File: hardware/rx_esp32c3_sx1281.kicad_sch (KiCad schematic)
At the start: 43 parts, among them U1 ESP32-C3FH4, U2 TLV75533PDQNR, U3 SX1281IMLTRT, X1 CJ17-400001010B20

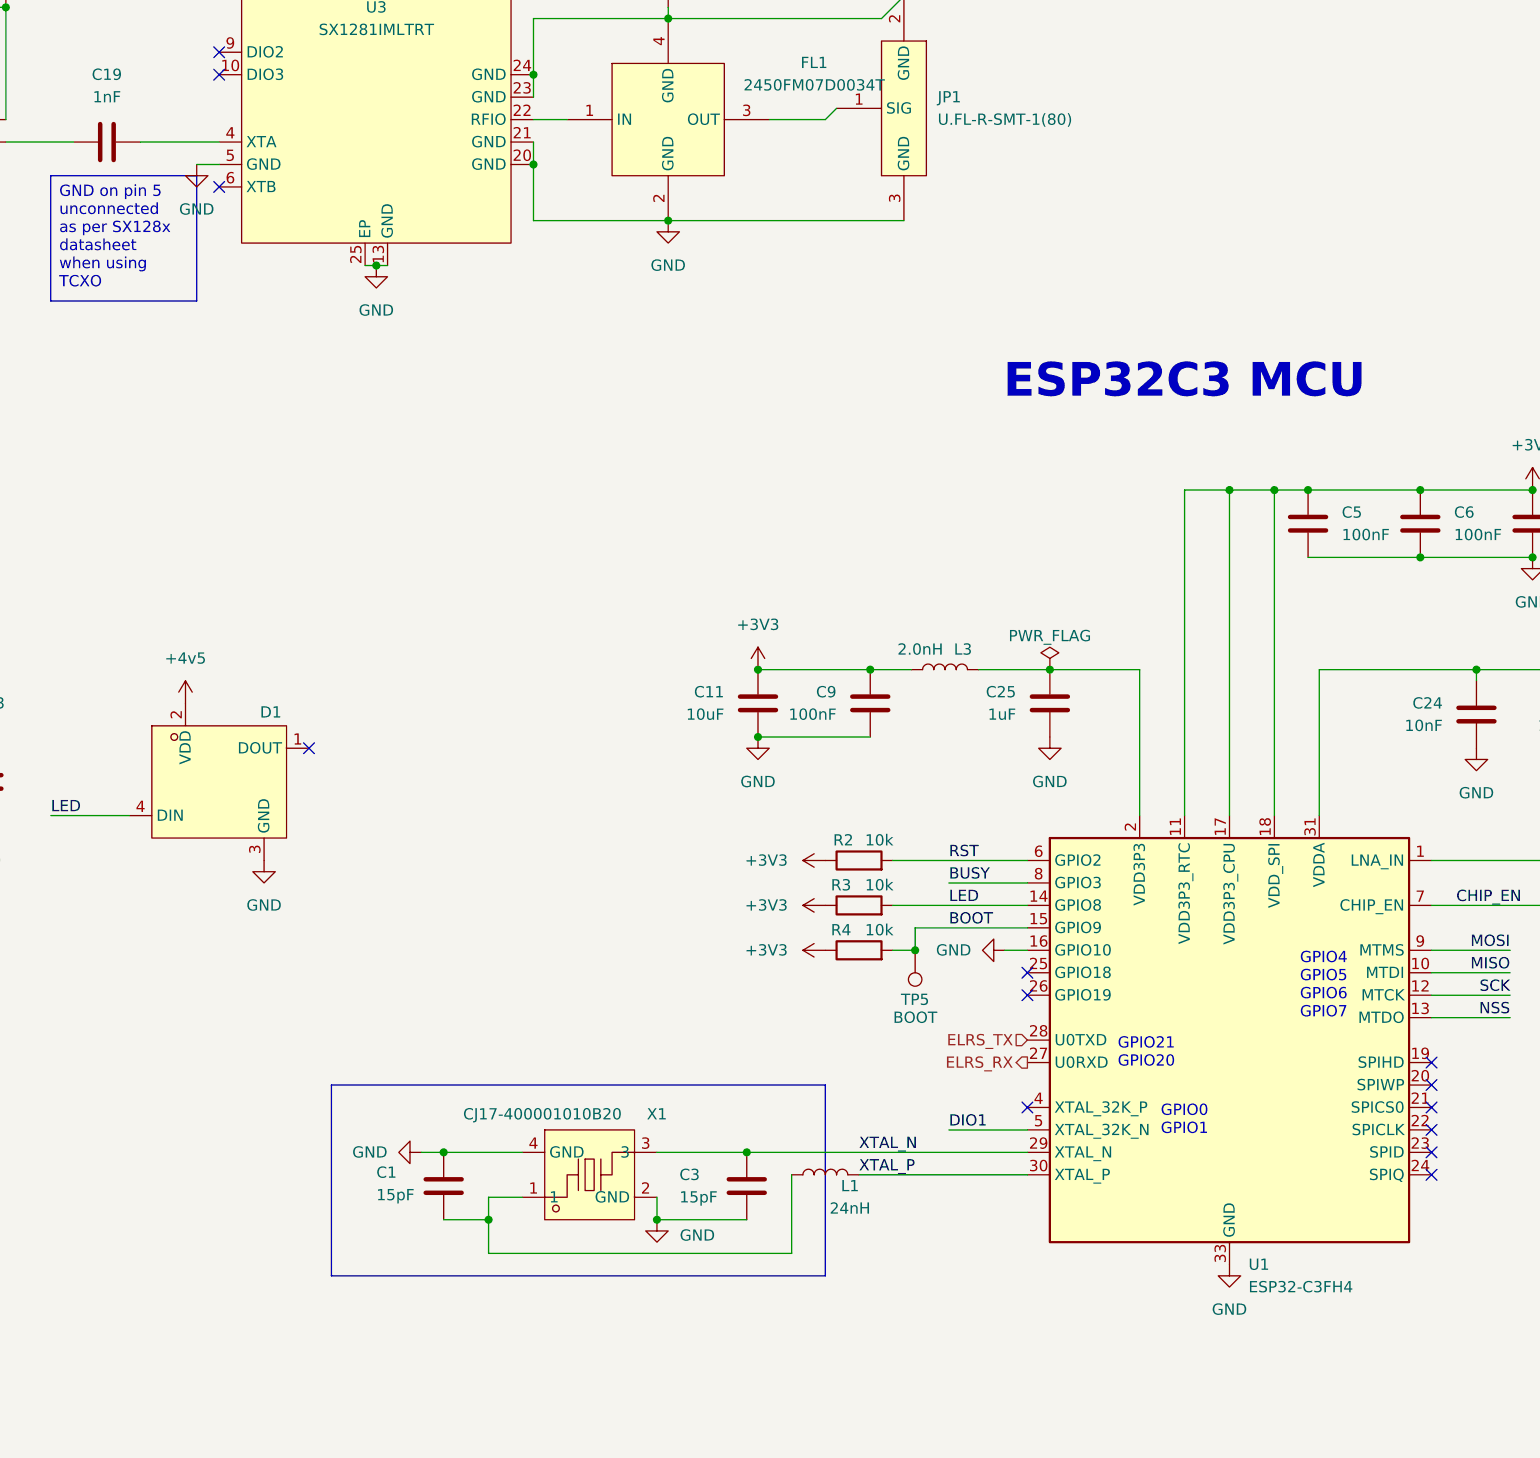
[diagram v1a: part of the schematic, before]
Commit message: One board from the owner's 2026-08-22 Base and Core, BMP580 baro (#26)
The board is rebuilt from d81e559 (the hand-routed Base recovered from KiCad
local history and the hand-routed Core of 1fe3d21) plus the always-on +10V of
9aba717, instead of the agent-reworked 8fa8d7b. Both layouts sit side by side
in hardware/OpenAIO.kicad_pcb with all routing kept (2513 tracks, 1577 vias),
on the OpenAIO-Whoop 8L HDI stackup.

- Schematic: Core_Interface (J90/J91 LGA) removed; U26 BMP580 + C107/C108 on
  I2C0 at 0x47 (Betaflight BMP5xx default). Netlist otherwise identical to
  9aba717; ERC 31 errors, the 9aba717 baseline.
- Board: Base netclasses and severities; rule area "Core layout" keeps the
  Core's 0.09 line standard. DRC: 3 errors (USB1 peg), 37 unconnected (links).
- lib.pretty footprints replaced by the board instances; BMP580 imported with
  easyeda2kicad (LCSC C22391138).
- Not carried from 8fa8d7b: TXU0101 LED-strip buffer, +3V3_ESC, SWD pads,
  DFM edits; firmware ISSUES I2/I3 reopened.
- Docs: README pinout re-measured, AGENTS.md, research/ROUTING.md, Betaflight
  target USE_BARO_BMP580.

Co-authored-by: Stan <stan@openaio.local>
Co-authored-by: Claude Opus 5.5 <noreply@anthropic.com>
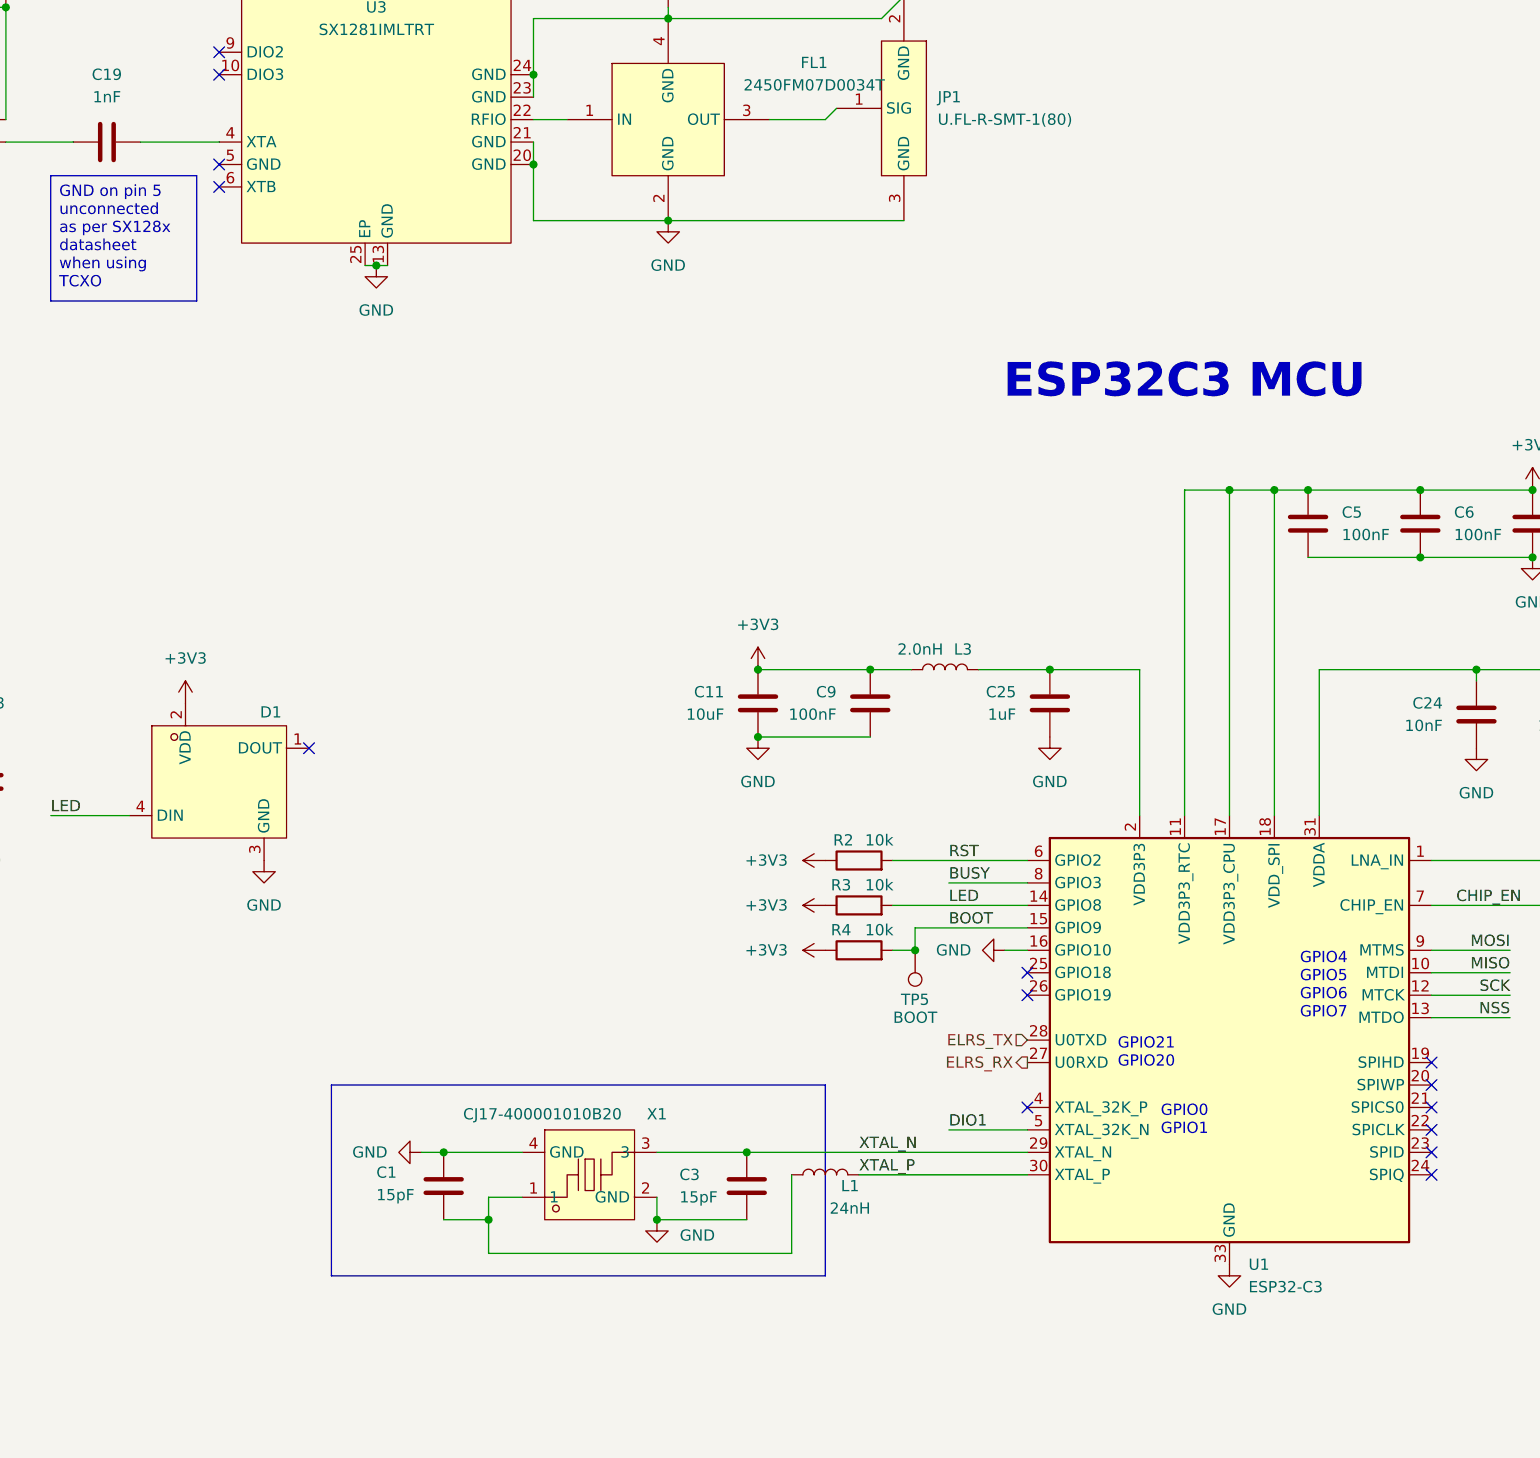
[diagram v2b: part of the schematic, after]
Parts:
- AE1: MPN 2450AT18A100E -> (none); Manufacturer JOHANSON(约翰逊) -> (none)
- C1, C3: MPN GRM0335C1H150JA01D -> (none); Manufacturer Murata Electronics -> (none)
- C10, C15, C23, C25, C28, C4: MPN GRM033R61A105ME44D -> (none); Manufacturer Murata Electronics -> (none)
- C11: MPN GRM155R60J106ME44D -> (none); Manufacturer Murata Electronics -> (none)
- C12, C13, C14, C17, C5, C6, C9: MPN GRM033R61E104KE14D -> (none); Manufacturer Murata Electronics -> (none)
- C16, C8: MPN CL05A106MQ5NUNC -> (none); Manufacturer Samsung Electro-Mechanics -> (none)
- C19: MPN 0201B102K500NT -> (none); Manufacturer FH (Guangdong Fenghua) -> (none)
- C20: MPN GRM033R60J474KE90D -> (none); Manufacturer Murata Electronics -> (none)
- C21, C22: MPN GRM0335C1H1R2BA01D -> (none); Manufacturer Murata Electronics -> (none)
- C24, C26, C27: MPN GRM033R61A103KA01J -> (none); Manufacturer Murata Electronics -> (none)
- D1: LCSC C5349953 -> (none); MPN XL-1010RGBC-2812B -> (none); Manufacturer XINGLIGHT -> (none)
- JP1: MPN U.FL-R-SMT-1(80) -> (none); Manufacturer Hirose -> (none)
- L1: MPN LQP03TN24NH02D -> (none); Manufacturer Murata Electronics -> (none)
- L2: MPN LQP03TN2N5C02D -> (none); Manufacturer Murata Electronics -> (none)
- L3: MPN LQP03TN2N0B02D -> (none); Manufacturer Murata Electronics -> (none)
- L4: LCSC C383402 -> (none); MPN MLZ2012M150WT000 -> (none); Manufacturer TDK -> (none)
- OSC1: MPN OW7EL89CENUNFAYLC-52M -> (none); Manufacturer TXC -> (none)
- R2, R3, R4, R5: MPN RC0201FR-0710KL -> (none); Manufacturer YAGEO -> (none)
- TP5: now in the parts list
- U1: value ESP32-C3FH4 -> ESP32-C3; LCSC C2858491 -> (none); MPN ESP32-C3FH4 -> (none); Manufacturer Espressif Systems -> (none)
- U2: MPN TLV75533PDQNR -> (none); Manufacturer Texas Instruments -> (none)
- U3: MPN SX1281IMLTRT -> (none); Manufacturer Semtech -> (none)
- X1: MPN CJ17-400001010B20 -> (none); Manufacturer Jiangsu Changjing Electronics -> (none)
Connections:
- net +3V3: now also D1.2 (VDD)
- net +4v5: no longer D1.2 (VDD)
- net GND: no longer U3.5 (GND)
- no-connect marks 14 -> 15

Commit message: Library: every symbol, footprint and 3D model project-local (#28)
* Owner: board cleanup, Core placed on the board

Co-Authored-By: Claude Opus 5.5 <noreply@anthropic.com>

* Library: every symbol, footprint and 3D model project-local

- 3D models: 275 board model paths and 28 lib.pretty footprints pointed at
  KiCad's stock install or at ${OPENDRONE_LIB} (which this machine's KiCad sets
  to a path that does not exist, so 9 models were missing). All now resolve to
  ${KIPRJMOD}/lib.3dshapes; the three missing ones come from the repo's
  KiCad-Library submodule. .wrl replaced by the .step sibling where one exists.
- Symbols: the 14 stock symbols (Device, power, Connector, Connector_Generic,
  MCU_Espressif) copied into lib.kicad_sym from the schematic's own cache and
  relinked as lib:. Four lib symbols refreshed from the schematic (they still
  held the 8fa8d7b copies).
- Pruned: 11 unused footprints, 7 unused symbols, unreferenced model files.
- tools/localise_models.py and tools/localise_symbols.py keep it that way.
- Checks: board diff is model lines only; netlist identical; ERC 31 errors as
  before, lib_symbol_mismatch 9 -> 0.

Co-Authored-By: Claude Opus 5.5 <noreply@anthropic.com>

---------

Co-authored-by: Stan <stan@openaio.local>
Co-authored-by: Claude Opus 5.5 <noreply@anthropic.com>
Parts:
- C1, C10, C11, C12, C13, C14, C15, C16, C17, C19, C20, C21, C22, C23, C24, C25, C26, C27, C28, C3, C4, C5, C6, C8, C9: symbol Device:C -> lib:C
- L1, L2, L3, L4: symbol Device:L -> lib:L
- R2, R3, R4, R5: symbol Device:R -> lib:R
- TP5: symbol Connector:TestPoint -> lib:TestPoint
- U1: symbol MCU_Espressif:ESP32-C3 -> lib:ESP32-C3

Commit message: Owner: rerouting in progress; KiCad re-save of the sheets (netlist unchanged)
Co-Authored-By: Claude Opus 5.5 <noreply@anthropic.com>
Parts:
- renumbered AE1 to AE2, C13 to C65, C12 to C66, C26 to C67, C20 to C68, C19 to C69, C14 to C70, C17 to C71, C1 to C72, C27 to C73, C3 to C74, C11 to C75, C9 to C76, C25 to C77, C5 to C78, C6 to C79, C24 to C80, C23 to C81, C8 to C82, C4 to C83, C28 to C84, C10 to C85, C15 to C86, C22 to C87, C16 to C88, C21 to C89, D1 to D9, L1 to L5, L3 to L6, L2 to L7, R2 to R111, R3 to R112, R4 to R113, R5 to R114, TP5 to TP9, U3 to U21, U1 to U22, U2 to U23, X1 to X2

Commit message: One 3.3 V rail: U7 becomes TLV76733DRVR (1 A), U23 removed
- U7 LP5912-3.3DRVR (500 mA) -> TLV76733DRVR (1 A, LCSC C2848334, as on
  OpenESC-20x20), same WSON-6 2x2 land; SNS (pin 2) tied to OUT in the
  schematic and by a 0.25 mm jumper on B.Cu.
- U23 TLV75533 removed; the 17 +3V3 power symbols are +3.3V, and the board's
  +3V3 copper (24 tracks, 6 vias, 3 pours) moved onto +3.3V.
- Netlist: only U7 (value, MPN, LCSC, pin 2), U23 gone, +3V3 merged into +3.3V.
  ERC 31 errors as before. DRC: no new unconnected beyond the link the old
  +3V3 side now needs to U7.
- Docs: ROUTING.md rails and reroute step; firmware notes on the single rail
  (ISSUES I15 resolved).

Co-Authored-By: Claude Opus 5.5 <noreply@anthropic.com>
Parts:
- removed U23: TLV75533PDQNR, lib:X2SON-4_L1.0-W1.0-P0.65-TL-EP, symbol lib:TLV75533PDQNR
- renumbered AE2 to AE1, C72 to C1, C85 to C10, C75 to C11, C66 to C12, C65 to C13, C70 to C14, C86 to C15, C88 to C16, C71 to C17, C69 to C19, C68 to C20, C89 to C21, C87 to C22, C81 to C23, C80 to C24, C77 to C25, C67 to C26, C73 to C27, C84 to C28, C74 to C3, C83 to C4, C78 to C5, C79 to C6, C82 to C8, C76 to C9, D9 to D1, L5 to L1, L7 to L2, L6 to L3, R111 to R2, R112 to R3, R113 to R4, R114 to R5, TP9 to TP5, U22 to U1, U21 to U3, X2 to X1
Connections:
- net +3V3 renamed +3.3V

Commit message: ELRS_EN on GPIO27, SWD test pads TP42/TP43
- GPIO27 (U2.41) -> ESP32-C3 CHIP_EN (net ELRS_EN; R114 keeps ELRS on).
  Betaflight PINIO1 (inverted push-pull) holds ELRS in reset on demand, so
  the DJI SBUS on SH-6 pin 6 can own UART1_RX.
- SWCLK (U2.24) -> TP42, SWDIO (U2.25) -> TP43, D1.0 pads, parked right of
  the outline for placement.
- tools/sch_debug_pins.py (sexpdata); netlist diff: only these nets change.
- Board synced: 0 DRC errors, unconnected 70 -> 72 (ELRS_EN, SWDIO).
  U2 pad 24 (SWCLK) is still missing: pad 23 (+1.1V) cannot escape past XOUT/C4
  and the +3.3V via under it; needs a hand rework of the crystal corner.

Co-Authored-By: Claude Opus 5.5 <noreply@anthropic.com>
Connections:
- net CHIP_EN renamed ELRS_EN
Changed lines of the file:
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@@
+		)
+	)
+	(global_label "ELRS_EN"
+		(shape bidirectional)
+		(at 255.27 205.74 0)
+		(effects
+			(font
+				(size 1.27 1.27)
+			)
+			(justify left)
+		)
+		(property "Intersheetrefs" "${INTERSHEET_REFS}"
+			(at 255.27 205.74 180)
+			(hide yes)
+			(show_name no)
+			(do_not_autoplace no)
+			(effects
+				(font
+					(size 1.27 1.27)
+				)
+			)
 		)
 	)
